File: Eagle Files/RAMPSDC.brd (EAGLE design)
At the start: 99.1 x 59.7 mm, 20 parts, among them IC1 AT24CP, IC2 7805T, U1 ARDUINO_MEGA_SHIELD

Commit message: Fixed a critical issue with the Step-downs.
They are actually seperated by 5 pins, not 6. Derp! Fixed. I'm working
on a new revision that will get rid of the maximum endstops and servos
2-4 (disconnect completely), and use that spare driver to regulate an
LCD screen down, or at least make pinouts for an SD ramps
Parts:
- moved JP1 2.54 mm to (44.5, 28.9)
- moved JP3 2.54 mm to (27.9, 28.9)
- moved JP7 2.54 mm to (11.4, 28.9)
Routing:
- net +3.3V: track 179.7 -> 208.0 mm
- net LV_D9: track 40.3 -> 37.7 mm
- net LV_D4: track 29.1 -> 26.6 mm
- net LV_Z-MIN: track 53.6 -> 51.1 mm
- net LV_D6: track 26.6 -> 24.0 mm
- net LV_D11: track 35.5 -> 33.0 mm
- net LV_D10: track 32.5 -> 29.9 mm
- net LV_X-MIN: track 46.3 -> 43.8 mm
- net LV_D8: track 48.7 -> 46.1 mm
- net LV_D5: track 28.7 -> 26.4 mm
- net LV_Y-MAX: track 43.2 -> 41.3 mm
- net LV_Y-MIN: track 50.1 -> 49.0 mm
- net LV_X-MAX: track 57.4 -> 58.0 mm
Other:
- board text added: "V1.1"
- board text removed: "V1.0"

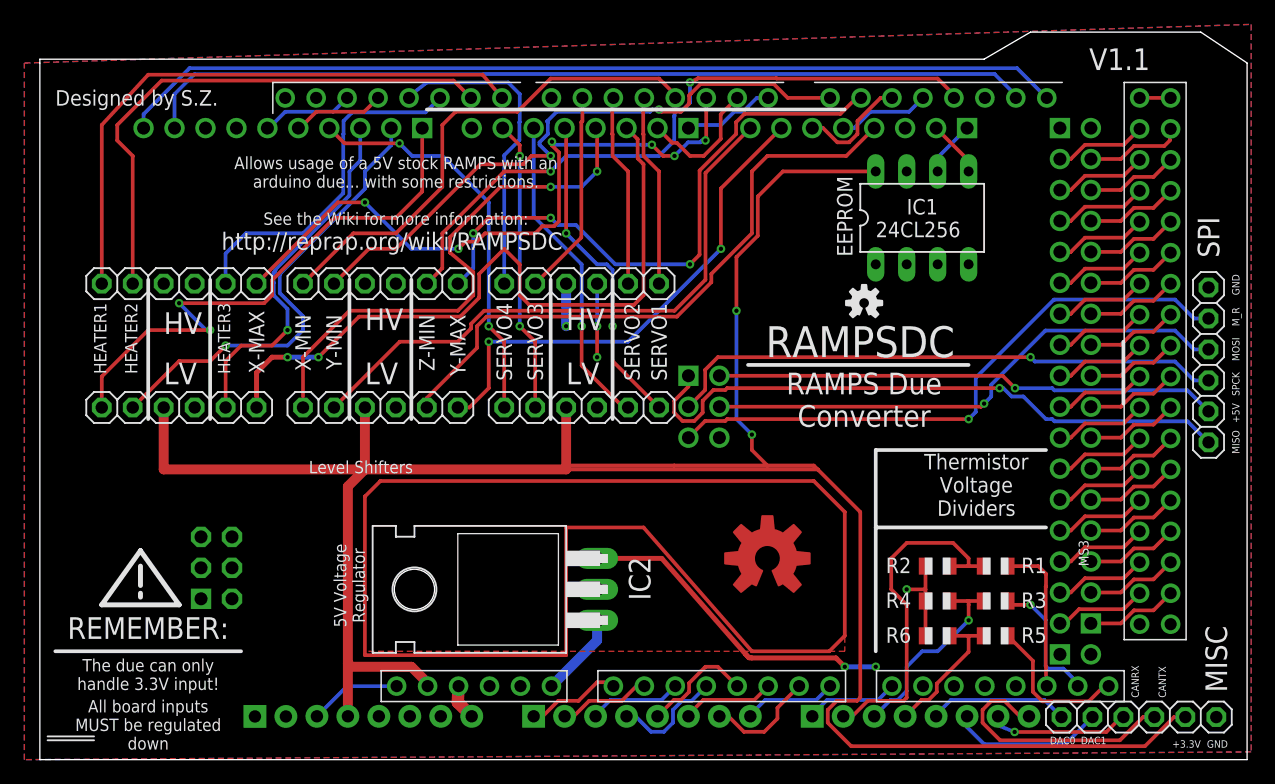
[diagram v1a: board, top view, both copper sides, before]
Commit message: Disconnected Max Endstops and Servos 2-4. Added SD card Headers. Fixed some Silkscreen errors.
This is a step towards making the LCD screen work, but in the meantime,
the last level shifter was changed to all NC. At some point, that will
be the encoder button, encoder 1, encoder 2, MISO, and whatever else
needs to be shifted to make the reprap full graphics controller work.
The issue is the documentation sucks on that so I need to really dig to
make it work. In the meantime, I added just a breakout header for the
generic 6-pin SD card module for arduinos. This doesnt replace an LCD,
but at least makes it run standalone.

The Max Endstops were not rerouted to anywhere, and are disconnected
from the rest of the system to prevent someone accidently frying their
Due. The Servo pins are outputs, so they were connected back the their
respective pins, but are not level shifted, so they may behave
strangely. The first Servo pin (SERVO0) is level shifted.
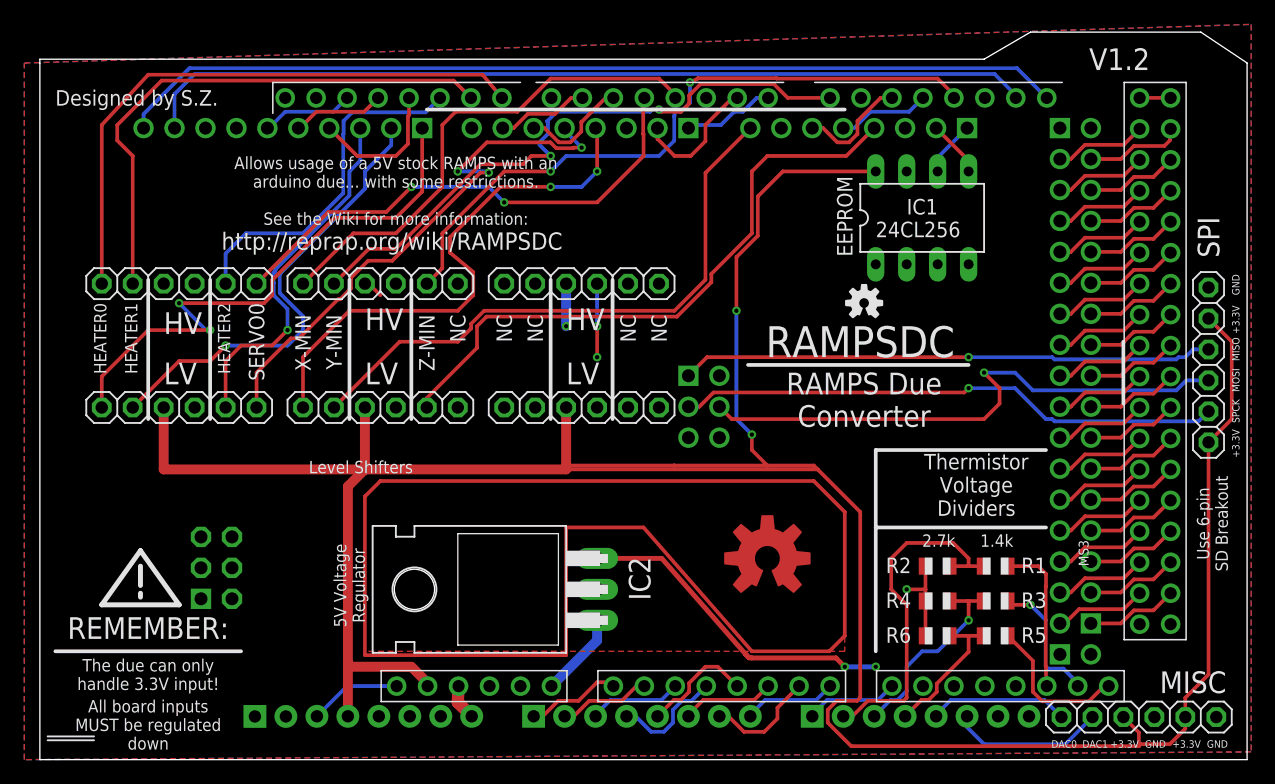
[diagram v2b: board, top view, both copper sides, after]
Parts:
- renumbered JP6 to JP9
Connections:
- removed net +5V: ARDUINO_DUE1.5V_2, JP9.2
- removed net LV_D11: ARDUINO_DUE1.11, JP1.1
- removed net LV_D5: ARDUINO_DUE1.5, JP1.5
- removed net LV_D6: ARDUINO_DUE1.6, JP1.2
- new net N$10: JP3.6
- new net N$11: JP4.6
- new net N$2: JP1.1
- new net N$3: JP1.2
- new net N$4: JP2.1
- new net N$5: JP2.2
- new net N$6: JP2.5
- new net N$7: JP2.6
- new net N$8: JP1.6
- new net N$9: JP1.5
- net +3.3V: now also JP5.3, JP9.1, JP9.5
- net CANRX: no longer JP5.3
- net CANTX: no longer JP5.4
- net D11: now also ARDUINO_DUE1.11; no longer JP2.1
- net D4: now also JP8.6; no longer JP2.6
- net D5: now also ARDUINO_DUE1.5; no longer JP2.5
- net D6: now also ARDUINO_DUE1.6; no longer JP2.2
- net GND: now also JP5.4
- net LV_D4: now also JP7.6; no longer JP1.6
- net LV_X-MAX: no longer JP7.6
- net LV_Y-MAX: no longer JP3.6
- net MASTER_R: no longer JP9.5
- net MISO: now also JP9.4; no longer JP9.1
- net MOSI: now also JP9.3; no longer JP9.4
- net SPCK: now also JP9.2; no longer JP9.3
- net X-MAX: no longer JP8.6
- net Y-MAX: no longer JP4.6
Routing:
- net LV_X-MAX: track 58.0 -> 0.00 mm, vias 2 -> 0
- net X-MAX: track 54.0 -> 0.00 mm, vias 6 -> 0
- net MASTER_R: track 49.6 -> 0.00 mm, vias 1 -> 0
- net Y-MAX: track 48.8 -> 0.00 mm, vias 3 -> 0
- net +5V: track 41.3 -> 0.00 mm, vias 1 -> 0
- net LV_Y-MAX: track 41.3 -> 0.00 mm, vias 2 -> 0
- net +3.3V: track 208.0 -> 246.5 mm
- net LV_D11: track 33.0 -> 0.00 mm, vias 2 -> 0
- net LV_D5: track 26.4 -> 0.00 mm, vias 1 -> 0
- net D4: track 15.8 -> 42.0 mm, vias 0 -> 2
- net LV_D6: track 24.0 -> 0.00 mm, vias 2 -> 0
- net CANTX: track 21.2 -> 0.00 mm
- net LV_D4: track 26.6 -> 45.3 mm, vias 2 -> 3
- net D11: track 26.1 -> 11.6 mm
- net CANRX: track 11.6 -> 0.00 mm, vias 1 -> 0
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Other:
- board text added: "1.4k"
- board text added: "2.7k"
- board text added: "HEATER0"
- board text added: "NC"
- board text added: "SERVO0"
- board text added: "Use 6-pin SD Breakout"
- board text added: "V1.2"
- board text removed: "+5V"
- board text removed: "CANRX"
- board text removed: "CANTX"
- board text removed: "HEATER3"
- board text removed: "M_R"
- board text removed: "SERVO1"
- board text removed: "SERVO2"
- board text removed: "SERVO3"
- board text removed: "SERVO4"
- board text removed: "V1.1"
- board text removed: "X-MAX"
- board text removed: "Y-MAX"
